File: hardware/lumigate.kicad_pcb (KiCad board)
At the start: 4 copper layers, 99 x 79 mm, 92 parts, among them J1 XLR-5 NC5FAH, J2 USB-C, J3 HY931147C, J4 DISP SH9, J5 XLR-5 NC5FAH, J6 EXP SH9, J7 DMX-OUT A, J8 DMX-OUT B, Q1 MMBT3904, Q2 MMBT3904, SW1 BOOT, SW2 RST, U1 ESP32-S3-WROOM-1-N8, U2 W5500, U3 CH340C, U4 SY8089, U5 ISO3086DWR, U6 ISO3086DWR, U7 DP9900M-5V, U8 USBLC6-2SC6, Y1 25MHz

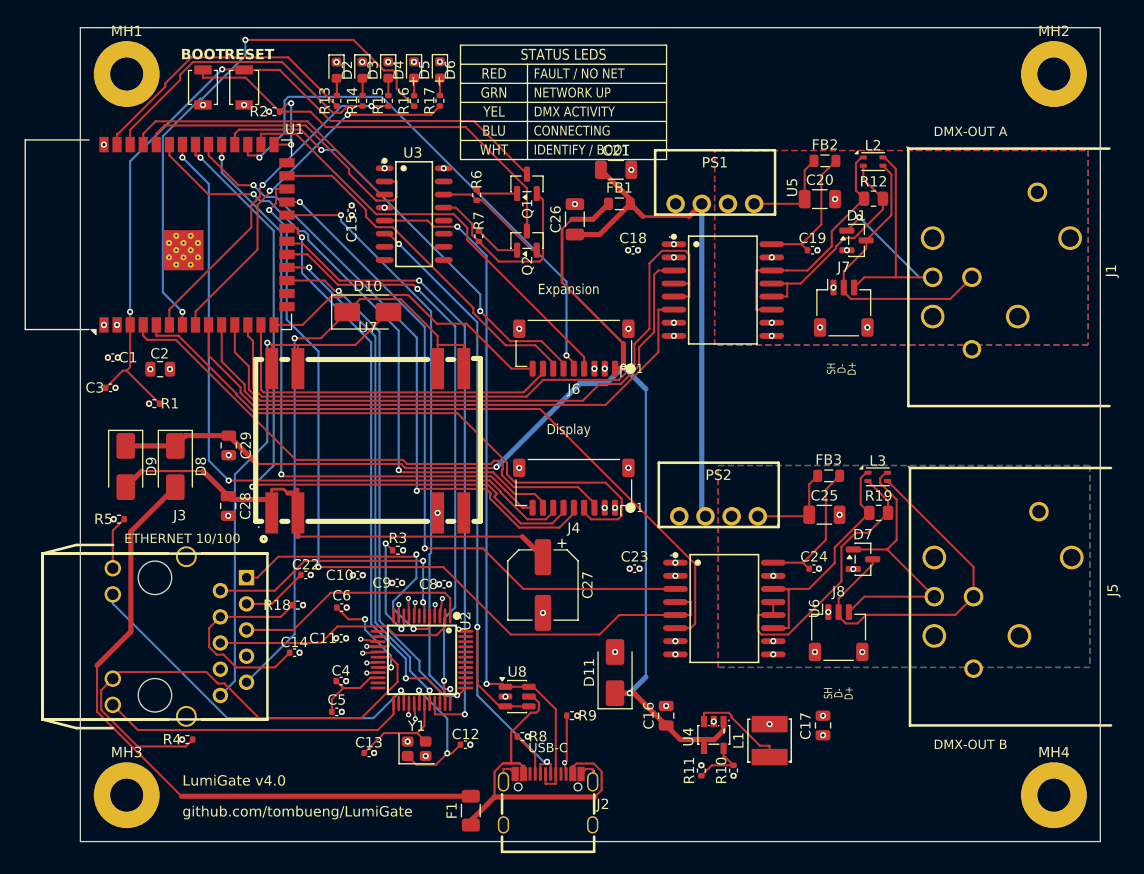
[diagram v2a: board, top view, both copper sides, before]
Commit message: hardware v4: back key-features grid + silk normalization + validator fixes
- back: added a gridded KEY FEATURES table (input, dual isolated output, datasheet-confirmed isolation
  values 1kV B0505S / 2.5kV ISO3086 / 1500V PoE, power, grounding "M3 screws to metal case", DMX shells
  off chassis).
- front: normalized every small-part reference designator to a consistent side (above the part, 0.8mm,
  4-side collision fallback) and added a function label to each big chip (ESP32-S3, W5500, USB-UART,
  3V3 buck, DMX1/DMX2 ISO485, PoE PD, B0505S ISO 5V, USB ESD).
- validators: updated validate_electrical.py to the real power chain (SS54 + PTC + ferrite, 33pF crystal,
  12.4k EXRES1) and validate_placement.py to the new net names (VISO_DRV / +5V_DMX / DMX_AO). Electrical
  now 14 PASS / 3 WARN / 0 FAIL.

0 unrouted; remaining silk is cosmetic (silk-over-copper, batch for the pre-fab cleanup).
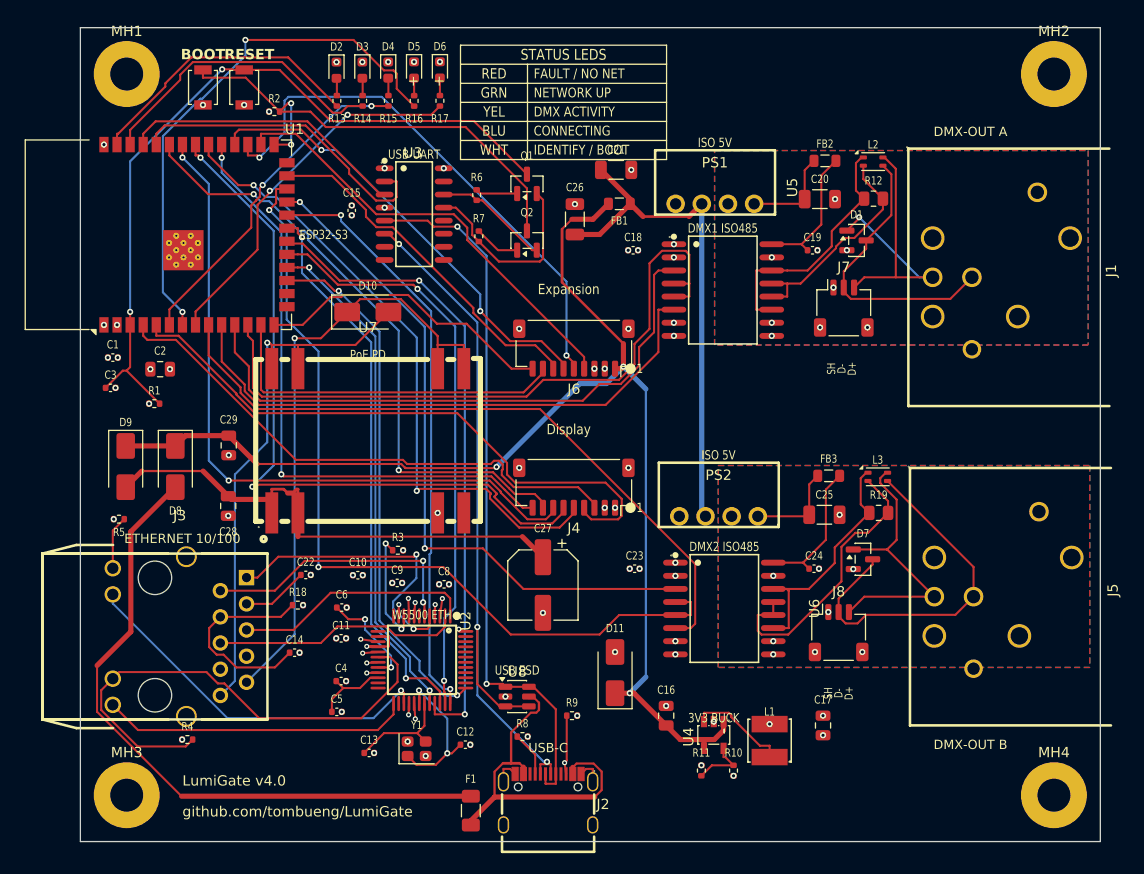
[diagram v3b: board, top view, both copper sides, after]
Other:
- board text added: "1kV galvanic (B0505S)"
- board text added: "2x isolated DMX512-A"
- board text added: "3V3 BUCK"
- board text added: "802.3af, 1500V iso"
- board text added: "Art-Net / sACN"
- board text added: "CORE"
- board text added: "DETAIL"
- board text added: "DMX ISO"
- board text added: "DMX SHELL"
- board text added: "DMX1 ISO485"
- board text added: "DMX2 ISO485"
- board text added: "ESP32-S3"
- board text added: "ESP32-S3 + W5500 10/100"
- board text added: "FEATURE"
- board text added: "GROUND"
- board text added: "INPUT"
- board text added: "ISO 5V"
- board text added: "ISO XCVR"
- board text added: "ISO3086 2.5kVrms"
- board text added: "LumiGate v4 -- KEY FEATURES"
- board text added: "M3 screws -> metal case"
- board text added: "OUTPUTS"
- board text added: "POWER"
- board text added: "PoE"
- board text added: "PoE PD"
- board text added: "USB ESD"
- board text added: "USB-C 5V or PoE (OR-ed)"
- board text added: "USB-UART"
- board text added: "W5500 ETH"
- board text added: "keep OFF chassis (iso)"

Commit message: hardware v4: TPS2116 ideal-diode OR + BOM/CPL completeness + fab fixes
Replace the USB/PoE OR diodes (D8/D9) with a TPS2116 ideal-diode mux (U9, C30/C31).
The ~0.4V Schottky drop pulled +5V low enough that the B0505S/ISO3086 VCC2 rail
dipped under its 4.5V min on USB power; the mux drop is ~30mV so VCC2 now clears
4.5V across the whole USB range (SPICE-verified). Report/VALIDATION and the
electrical model updated to match.

BOM/CPL: the BOM was silently dropping the ruggedization parts (F1, U8, D11, L2/L3,
FB1-3) and J6/J7/J8, and the CPL listed the mounting holes. All fixed, every one of
the 89 placed parts now has a real LCSC, the generator warns on any future gap, and
it emits a valid openpyxl .xlsx so a stale spreadsheet can't be uploaded again.

Silk: ref-des now sit adjacent to their parts (rotate/slide, never fly off),
DMX1/DMX2 became DMX-A/DMX-B, key-features grid moved off the J3 magjack THT pins.
C17 moved clear of the J8 plug, USB-C 3D model offset set to -95 mils.

Routing regenerated clean (0 unrouted, the usual W5500/USB-C clearance waivers).
New helpers: route_en, repair_gaps, csv_to_xlsx. Freerouting now runs GUI-visible.
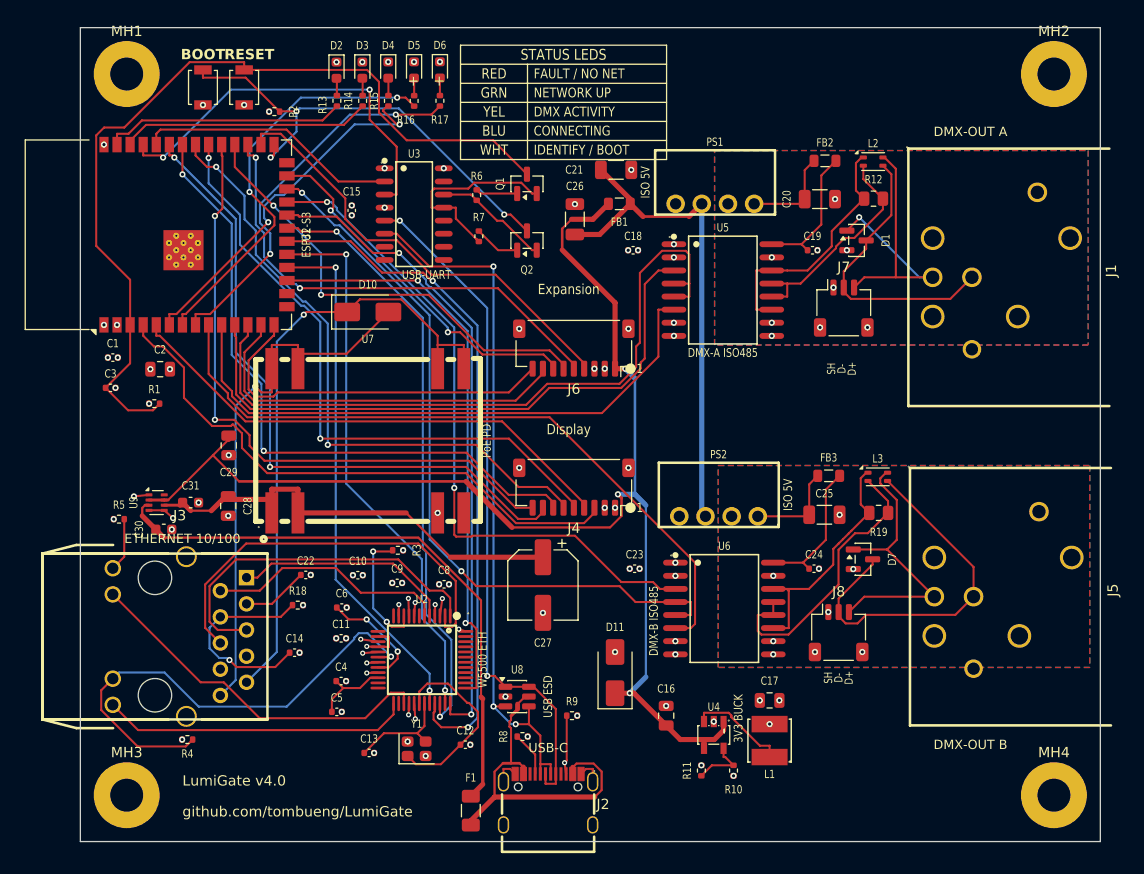
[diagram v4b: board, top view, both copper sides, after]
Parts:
- removed D8, D9: SS54, D_SMA
- added C30: 1uF, C_0603_1608Metric, F.Cu at (105.7, 137.6)
- added C31: 1uF, C_0603_1608Metric, F.Cu at (108.3, 135.0)
- added U9: TPS2116DRLR, SOT-583-8, F.Cu at (105.0, 135.0)
- moved C17 5.73 mm to (164.5, 154.2), turned to 0 degrees
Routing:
- net ETH_TXP: track 24.2 -> 40.1 mm
- net ETH_TXN: track 23.2 -> 35.1 mm
- net LED_B: track 51.8 -> 40.4 mm
- net DMX2_EN: track 82.4 -> 71.3 mm
- net EN: track 74.2 -> 84.7 mm, vias 2 -> 0
- net S3_TX: track 27.9 -> 38.3 mm, vias 0 -> 2
- net DISP_SCL: track 59.7 -> 49.7 mm
- net DISP_MOSI: track 70.6 -> 60.8 mm
- net ETH_RXN: track 29.1 -> 21.3 mm, vias 2 -> 0
- net +5V_USBF: track 64.6 -> 57.4 mm
- net EXP_IO20: track 29.3 -> 36.3 mm
- net +5V_POE: track 50.3 -> 44.5 mm
- net EXP_IO36: track 52.5 -> 46.7 mm
- net ETH_INT: track 57.6 -> 63.3 mm
- net S3_RX: track 30.8 -> 25.5 mm
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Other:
- board text added: "DMX-A ISO485"
- board text added: "DMX-B ISO485"
- board text removed: "DMX1 ISO485"
- board text removed: "DMX2 ISO485"

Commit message: hardware v4: full re-route to best outcome (0 unrouted, 3 waivers, EN auto-routed)
With U9 GND now pre-fanned by rebuild_iso, re-ran the whole pipeline (rebuild_iso -> escape_connectors -> autoroute_fr2 -> cleanup_pads -> tighten_poe_void -> widen_power). EN routed itself this pass: the freed congestion meant Freerouting no longer needed the manual route_en haul, so the board is fully routed with zero hand-stitching.

DRC: 0 unrouted, 3 clearance waivers (2x W5500 0.5mm-pitch escapes at 0.174mm, USB-C CC2 at 0.160mm, all >= JLCPCB 0.089mm min). The old +5V_POE/U7 GND near-miss is gone. Power traces widened to 0.5mm, PoE TH-pin moat carved + inner planes refilled.

Gerbers regenerated (14 files); BOM 89 parts / 0 to hand-pick; CPL 89, BOM<->CPL consistent. autoroute_fr2 timeout is now env-configurable (FR2_TIMEOUT) so a long optimisation session isn't cut off mid-route.
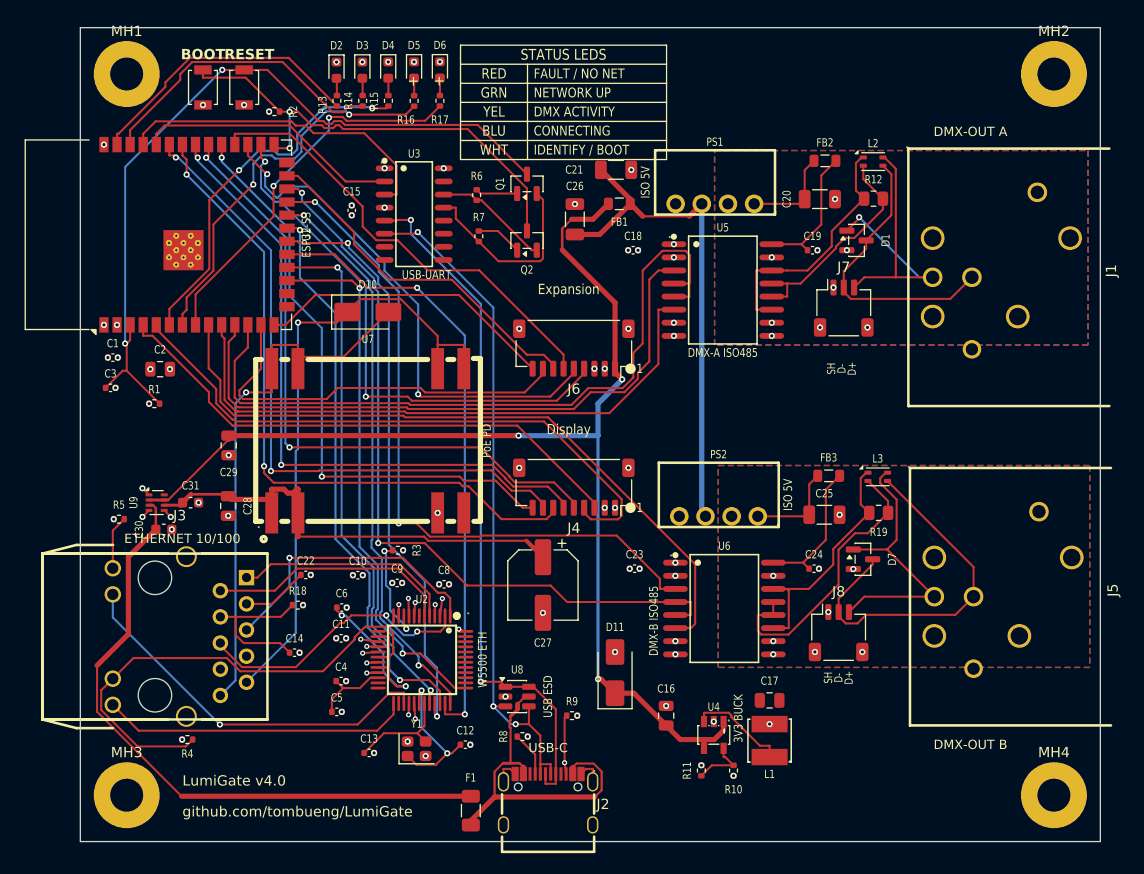
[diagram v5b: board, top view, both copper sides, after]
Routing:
- net ETH_TXP: track 40.1 -> 27.3 mm, vias 0 -> 2
- net +5V: track 127.1 -> 115.7 mm
- net DISP_SCL: track 49.7 -> 59.4 mm
- net SCLK: track 66.5 -> 56.9 mm
- net EXP_IO35: track 43.3 -> 52.3 mm, vias 0 -> 2
- net EN: track 84.7 -> 76.5 mm, vias 0 -> 2
- net ETH_INT: track 63.3 -> 55.4 mm
- net ETH_TXN: track 35.1 -> 27.7 mm, vias 0 -> 1
- net EXP_IO20: track 36.3 -> 29.3 mm
- net MOSI: track 53.3 -> 60.3 mm
- net S3_TX: track 38.3 -> 31.9 mm, vias 2 -> 0
- net +5V_USBF: track 57.4 -> 62.6 mm
- net LED_G: track 24.3 -> 29.3 mm
- net ETH_TCT: track 20.1 -> 15.2 mm, vias 1 -> 0
- net EXP_IO36: track 46.7 -> 51.2 mm
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
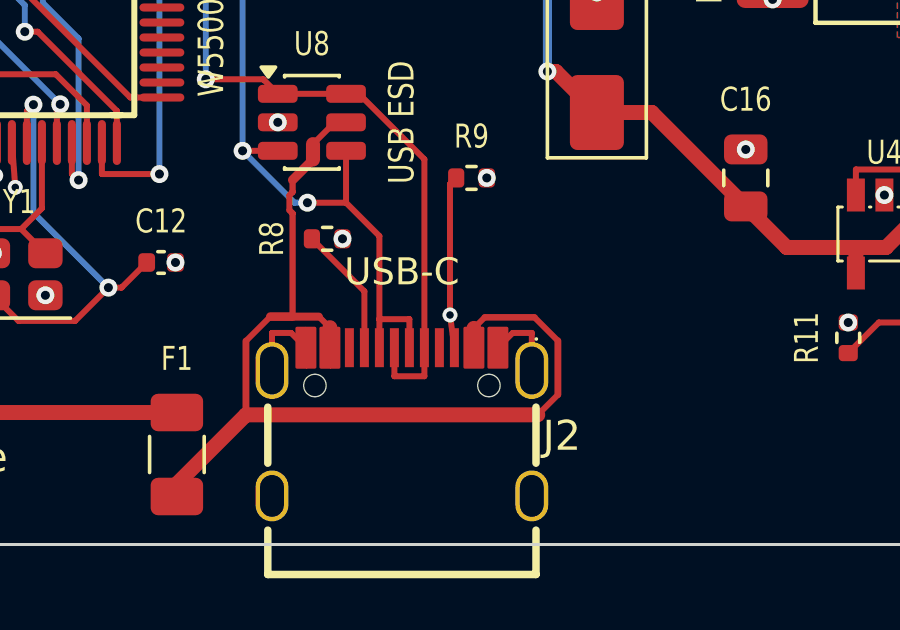
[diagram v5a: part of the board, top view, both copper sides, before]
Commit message: hardware v4: drop redundant CC2 escape via + silk DRC re-verify
Freerouting routed CC2 entirely on F.Cu, so the locked B.Cu escape via that escape_connectors placed for it ended up connected on only one layer (via_dangling). Removed it; CC2 stays connected through the F.Cu junction (0 unconnected, 0 dangling vias). Gerbers regenerated.

Silk DRC re-verified on the re-routed board: 0 silk-over-pad, 0 courtyard overlaps; 37 cosmetic warnings (16 near-edge, 15 silk-on-silk, 6 over-copper), all mask-protected. Validation doc counts updated to match.
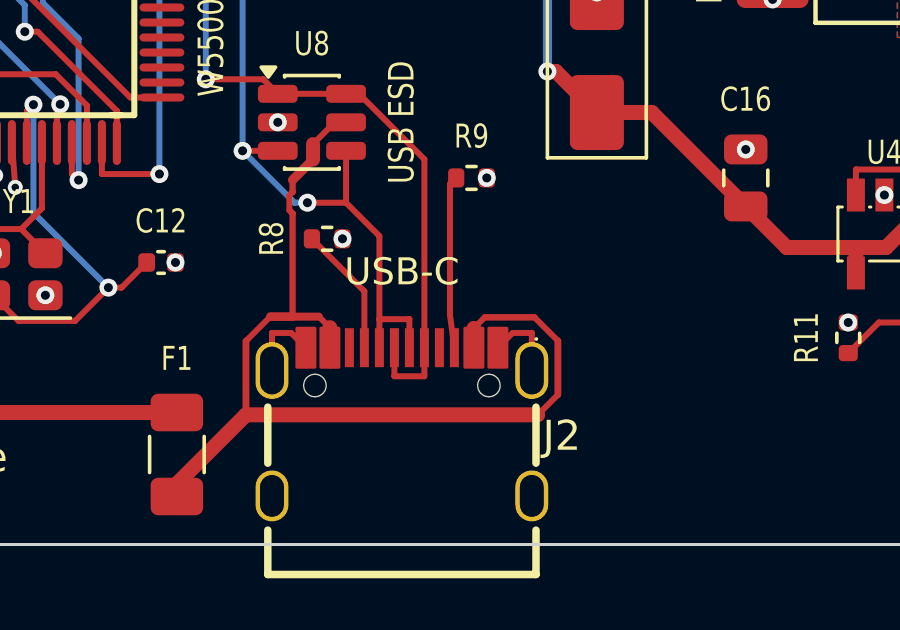
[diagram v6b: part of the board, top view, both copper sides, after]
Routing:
- net CC2: vias 1 -> 0
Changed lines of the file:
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@@
-		(net "CC2")
-	)
-	(via
-		(at 144.603486 160.2498)
-		(size 0.5)
-		(drill 0.25)
-		(layers "F.Cu" "B.Cu")
-		(locked yes)
 		(net "CC2")
 	)
